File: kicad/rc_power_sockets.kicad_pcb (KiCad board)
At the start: 2 copper layers, 50 x 50 mm, 20 parts, among them IC1 ATTINY85, J1 PIR, J2 433MHZ, J3 433MHZ, P1 ICSP, P2 CONN_GND, Q1 NMOS, Q2 PMOS, SW1 SPST, U1 MCP1700T

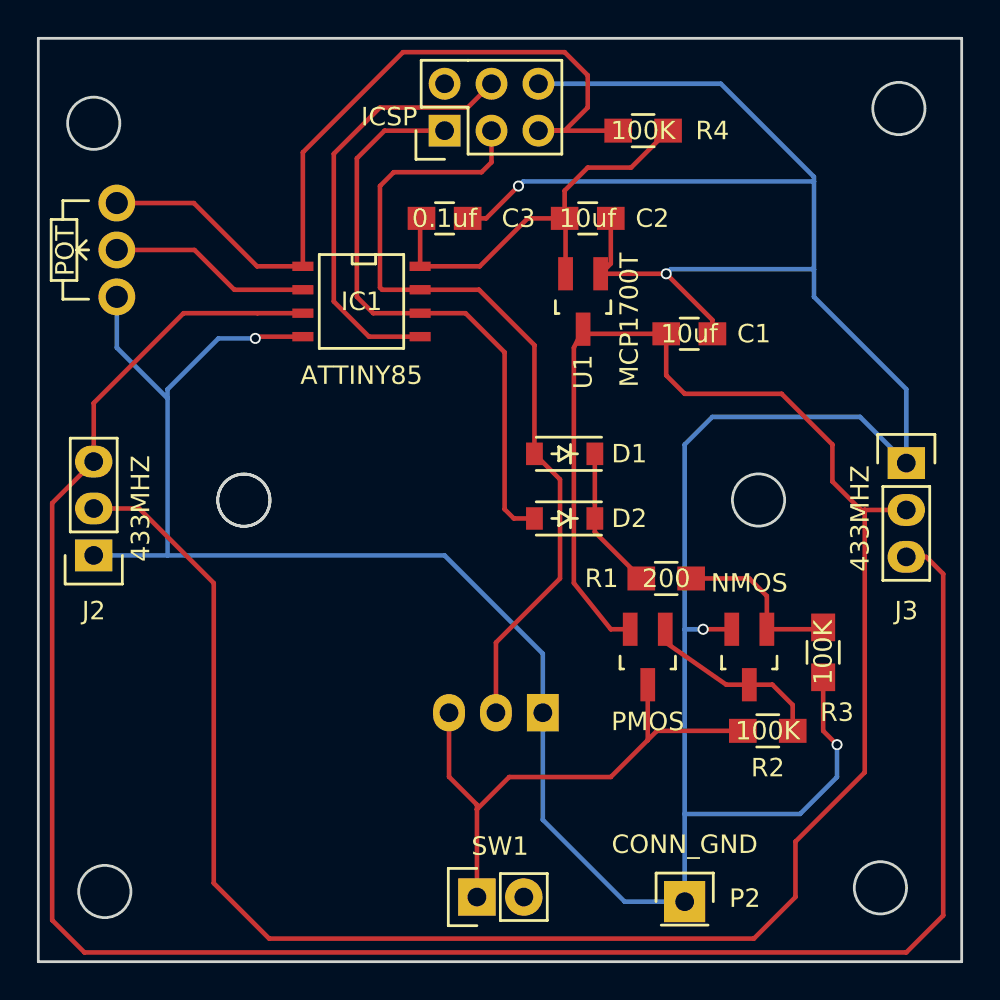
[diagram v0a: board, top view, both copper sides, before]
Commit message: Switched power plane
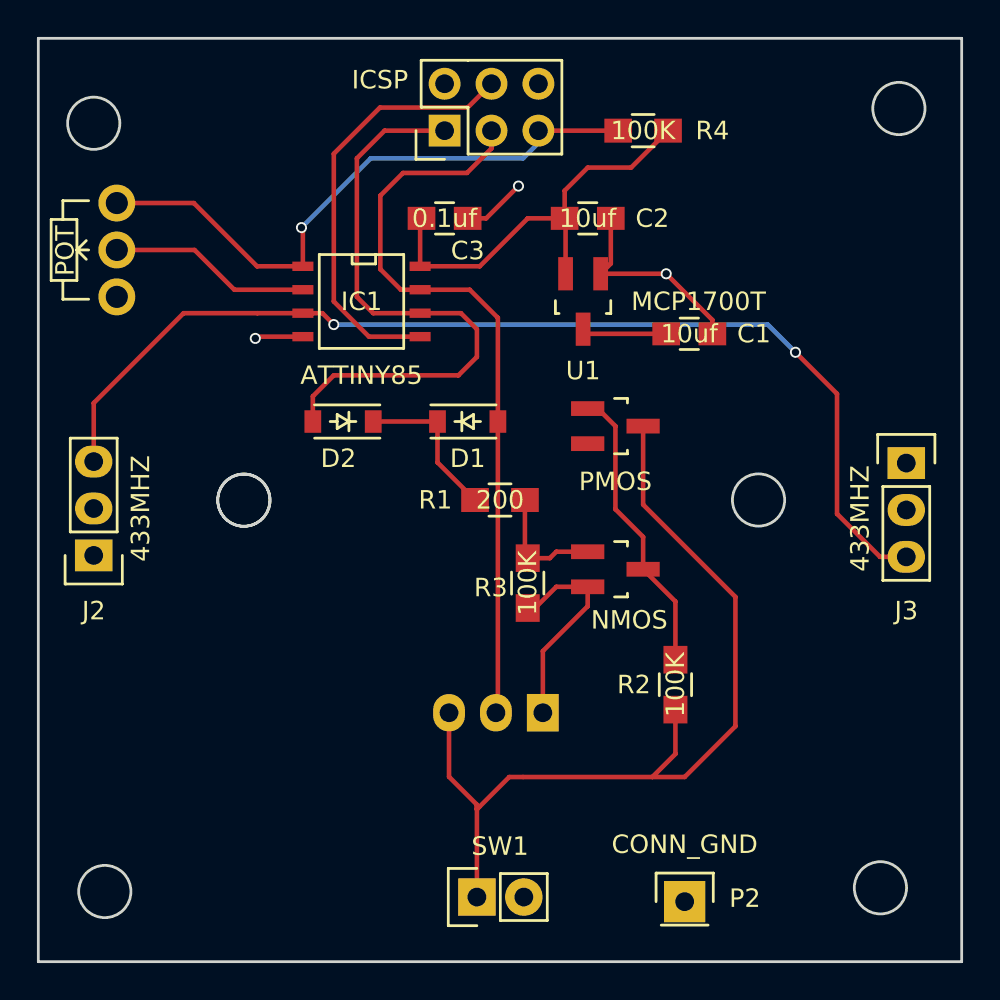
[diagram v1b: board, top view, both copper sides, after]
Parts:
- moved R3 16.4 mm to (146.5, 89.5)
- moved D2 13.1 mm to (136.5, 80.8)
- moved Q2 12.6 mm to (151.2, 81.0), turned to 270 degrees
- moved R1 9.95 mm to (145.0, 85.0)
- moved Q1 8.67 mm to (151.2, 88.8), turned to 270 degrees
- moved R2 5.59 mm to (154.5, 95.0), turned to 90 degrees
- moved D1 5.53 mm to (143.2, 80.8), turned to 0 degrees
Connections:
- P1 pad 2: /POWER -> /SWITCH_POWER
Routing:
- net GND: track 198.3 -> 28.7 mm, vias 5 -> 3
- net /SWITCH_POWER: track 122.9 -> 4.60 mm
- net /RADIO_DATA: track 113.0 -> 59.0 mm, vias 0 -> 2
- net /POWER: track 29.8 -> 49.2 mm
- net /RESET: track 45.1 -> 33.3 mm, vias 0 -> 1
- net /PBASE: track 10.2 -> 15.9 mm
- net /SCK: track 45.4 -> 40.9 mm
- net /NBASE: track 9.38 -> 6.61 mm
- net /NBASE_ON: track 7.79 -> 8.57 mm
- added copper zone on F.Cu, net /SWITCH_POWER
- added copper zone on B.Cu, net GND

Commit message: Mounting holes
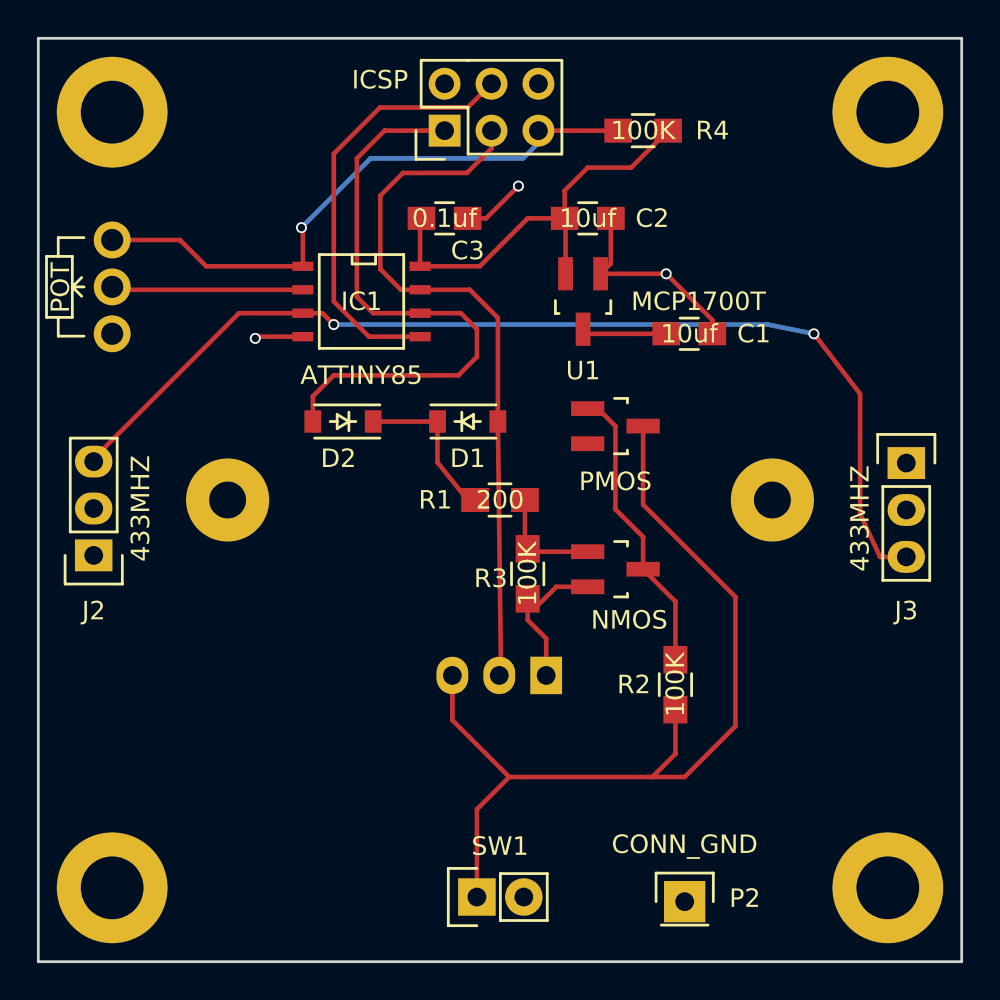
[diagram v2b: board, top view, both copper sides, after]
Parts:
- added REF**: SolderWirePad_single_2mmDrill, Wire_Pads:SolderWirePad_single_2mmDrill, F.Cu at (130.2, 85.0)
- added REF**: SolderWirePad_single_2-5mmDrill, Wire_Pads:SolderWirePad_single_2-5mmDrill, F.Cu at (124.0, 106.0)
- added REF**: SolderWirePad_single_2-5mmDrill, Wire_Pads:SolderWirePad_single_2-5mmDrill, F.Cu at (124.0, 64.0)
- added REF**: SolderWirePad_single_2-5mmDrill, Wire_Pads:SolderWirePad_single_2-5mmDrill, F.Cu at (166.0, 64.0)
- added REF**: SolderWirePad_single_2-5mmDrill, Wire_Pads:SolderWirePad_single_2-5mmDrill, F.Cu at (166.0, 106.0)
- added REF**: SolderWirePad_single_2mmDrill, Wire_Pads:SolderWirePad_single_2mmDrill, F.Cu at (159.8, 85.0)
- moved J1 2.03 mm to (147.5, 94.5)
- moved RV1 2.02 mm to (124.0, 76.0)
- moved R3 0.50 mm to (146.5, 89.0)
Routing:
- net GND: track 28.7 -> 25.4 mm
- net /SCK: track 40.9 -> 39.6 mm
- net /RADIO_DATA: track 59.0 -> 57.9 mm
- net /POWER: track 49.2 -> 49.9 mm
- net /NBASE: track 6.61 -> 6.02 mm
- net /RESET: track 33.3 -> 32.8 mm
- net /ADC3: track 11.0 -> 10.4 mm
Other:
- outline, holes or cut-outs redrawn

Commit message: Grounded mounting holes
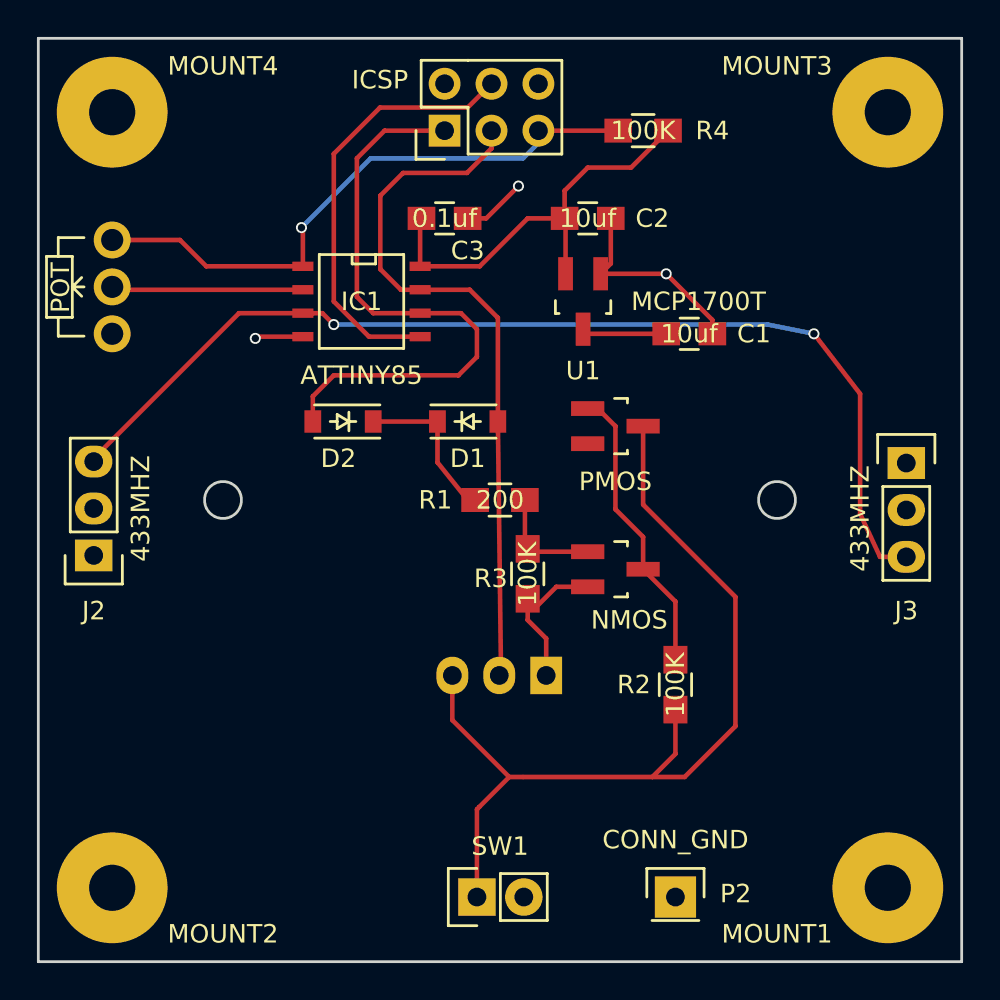
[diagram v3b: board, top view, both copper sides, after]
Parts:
- removed REF** (x2): SolderWirePad_single_2mmDrill, Wire_Pads:SolderWirePad_single_2mmDrill
- removed REF** (x4): SolderWirePad_single_2-5mmDrill, Wire_Pads:SolderWirePad_single_2-5mmDrill
- added MOUNT1: CONN_01X01, Wire_Pads:SolderWirePad_single_2-5mmDrill, F.Cu at (166.0, 106.0)
- added MOUNT2: CONN_01X01, Wire_Pads:SolderWirePad_single_2-5mmDrill, F.Cu at (124.0, 106.0)
- added MOUNT3: CONN_01X01, Wire_Pads:SolderWirePad_single_2-5mmDrill, F.Cu at (166.0, 64.0)
- added MOUNT4: CONN_01X01, Wire_Pads:SolderWirePad_single_2-5mmDrill, F.Cu at (124.0, 64.0)
- moved P2 0.56 mm to (154.5, 106.5)
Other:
- outline, holes or cut-outs redrawn
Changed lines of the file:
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@@
 (kicad_pcb (version 4) (host pcbnew 4.0.2-4+6225~38~ubuntu14.04.1-stable)
   (general
-    (links 42)
+    (links 46)
     (no_connects 0)
-    (area 112.185475 57.795 180.354525 112.055)
+    (area 118.375 59.924999 172.378334 112.055)
     (thickness 1.6)
-    (drawings 5)
+    (drawings 7)
     (tracks 117)
     (zones 0)
-    (modules 26)
+    (modules 24)
     (nets 15)
   )
@@
     (add_net VCC)
   )
-  (module Wire_Pads:SolderWirePad_single_2mmDrill (layer F.Cu)
-    (at 130.25 85)
-    (fp_text reference REF** (at 0 -3.81) (layer F.SilkS) hide
-      (effects (font (size 1 1) (thickness 0.15)))
-    )
-    (fp_text value SolderWirePad_single_2mmDrill (at -0.635 3.81) (layer F.Fab) hide
-      (effects (font (size 1 1) (thickness 0.15)))
-    )
-    (pad 1 thru_hole circle (at 0 0) (size 4.50088 4.50088) (drill 1.99898) (layers *.Cu *.Mask F.SilkS))
-  )
-  (module Wire_Pads:SolderWirePad_single_2-5mmDrill (layer F.Cu)
-    (at 124 106)
-    (fp_text reference REF** (at 0 -5.08) (layer F.SilkS) hide
-      (effects (font (size 1 1) (thickness 0.15)))
-    )
-    (fp_text value SolderWirePad_single_2-5mmDrill (at 1.27 5.08) (layer F.Fab) hide
-      (effects (font (size 1 1) (thickness 0.15)))
-    )
-    (pad 1 thru_hole circle (at 0 0) (size 5.99948 5.99948) (drill 3.4) (layers *.Cu *.Mask F.SilkS))
-  )
-  (module Wire_Pads:SolderWirePad_single_2-5mmDrill (layer F.Cu)
-    (at 124 64)
-    (fp_text reference REF** (at 0 -5.08) (layer F.SilkS) hide
-      (effects (font (size 1 1) (thickness 0.15)))
-    )
-    (fp_text value SolderWirePad_single_2-5mmDrill (at 1.27 5.08) (layer F.Fab) hide
-      (effects (font (size 1 1) (thickness 0.15)))
-    )
-    (pad 1 thru_hole circle (at 0 0) (size 5.99948 5.99948) (drill 3.4) (layers *.Cu *.Mask F.SilkS))
-  )
-  (module Wire_Pads:SolderWirePad_single_2-5mmDrill (layer F.Cu)
-    (at 166 64)
-    (zone_connect 1)
-    (fp_text reference REF** (at 0 -5.08) (layer F.SilkS) hide
-      (effects (font (size 1 1) (thickness 0.15)))
-    )
-    (fp_text value SolderWirePad_single_2-5mmDrill (at 1.27 5.08) (layer F.Fab) hide
-      (effects (font (size 1 1) (thickness 0.15)))
-    )
-    (pad 1 thru_hole circle (at 0 0) (size 5.99948 5.99948) (drill 3.4) (layers *.Cu *.Mask F.SilkS)
-      (zone_connect 1))
-  )
   (module TO_SOT_Packages_SMD:SOT-23_Handsoldering (layer F.Cu)
     (at 151.25 88.75 270)
@@
   )
   (module Pin_Headers:Pin_Header_Straight_1x01 (layer F.Cu)
-    (at 155 106.75)
+    (at 154.5 106.5)
     (descr "Through hole pin header")
     (tags "pin header")
@@
   (module Wire_Pads:SolderWirePad_single_2-5mmDrill (layer F.Cu)
     (at 166 106)
-    (fp_text reference REF** (at 0 -5.08) (layer F.SilkS) hide
-      (effects (font (size 1 1) (thickness 0.15)))
-    )
-    (fp_text value SolderWirePad_single_2-5mmDrill (at 1.27 5.08) (layer F.Fab) hide
-      (effects (font (size 1 1) (thickness 0.15)))
-    )
-    (pad 1 thru_hole circle (at 0 0) (size 5.99948 5.99948) (drill 3.4) (layers *.Cu *.Mask F.SilkS))
-  )
-  (module Wire_Pads:SolderWirePad_single_2mmDrill (layer F.Cu)
-    (at 159.75 85)
-    (fp_text reference REF** (at 0 -3.81) (layer F.SilkS) hide
-      (effects (font (size 1 1) (thickness 0.15)))
-    )
-    (fp_text value SolderWirePad_single_2mmDrill (at -0.635 3.81) (layer F.Fab) hide
-      (effects (font (size 1 1) (thickness 0.15)))
-    )
-    (pad 1 thru_hole circle (at 0 0) (size 4.50088 4.50088) (drill 1.99898) (layers *.Cu *.Mask F.SilkS))
-  )
+    (fp_text reference MOUNT1 (at -6 2.5) (layer F.SilkS)
+      (effects (font (size 1 1) (thickness 0.15)))
+    )
+    (fp_text value CONN_01X01 (at 1.27 5.08) (layer F.Fab) hide
+      (effects (font (size 1 1) (thickness 0.15)))
+    )
+    (pad 1 thru_hole circle (at 0 0) (size 5.99948 5.99948) (drill 2.49936) (layers *.Cu *.Mask F.SilkS)
+      (net 1 GND))
+  )
+  (module Wire_Pads:SolderWirePad_single_2-5mmDrill (layer F.Cu)
+    (at 124 106)
+    (fp_text reference MOUNT2 (at 6 2.5) (layer F.SilkS)
+      (effects (font (size 1 1) (thickness 0.15)))
+    )
+    (fp_text value CONN_01X01 (at 1.27 5.08) (layer F.Fab) hide
+      (effects (font (size 1 1) (thickness 0.15)))
+    )
+    (pad 1 thru_hole circle (at 0 0) (size 5.99948 5.99948) (drill 2.49936) (layers *.Cu *.Mask F.SilkS)
+      (net 1 GND))
+  )
+  (module Wire_Pads:SolderWirePad_single_2-5mmDrill (layer F.Cu)
+    (at 166 64)
+    (fp_text reference MOUNT3 (at -6 -2.5) (layer F.SilkS)
+      (effects (font (size 1 1) (thickness 0.15)))
+    )
+    (fp_text value CONN_01X01 (at 1.27 5.08) (layer F.Fab) hide
+      (effects (font (size 1 1) (thickness 0.15)))
+    )
+    (pad 1 thru_hole circle (at 0 0) (size 5.99948 5.99948) (drill 2.49936) (layers *.Cu *.Mask F.SilkS)
+      (net 1 GND))
+  )
+  (module Wire_Pads:SolderWirePad_single_2-5mmDrill (layer F.Cu)
+    (at 124 64)
+    (fp_text reference MOUNT4 (at 6 -2.5) (layer F.SilkS)
+      (effects (font (size 1 1) (thickness 0.15)))
+    )
+    (fp_text value CONN_01X01 (at 1.27 5.08 90) (layer F.Fab) hide
+      (effects (font (size 1 1) (thickness 0.15)))
+    )
+    (pad 1 thru_hole circle (at 0 0) (size 5.99948 5.99948) (drill 2.49936) (layers *.Cu *.Mask F.SilkS)
+      (net 1 GND))
+  )
+  (gr_circle (center 130 85) (end 130 84) (layer Edge.Cuts) (width 0.15))
+  (gr_circle (center 160 85) (end 160 84) (layer Edge.Cuts) (width 0.15))
   (gr_line (start 120 85) (end 170 85) (angle 90) (layer B.SilkS) (width 0.2))
   (gr_line (start 120 110) (end 120 60) (angle 90) (layer Edge.Cuts) (width 0.15))

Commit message: Labels on connectors
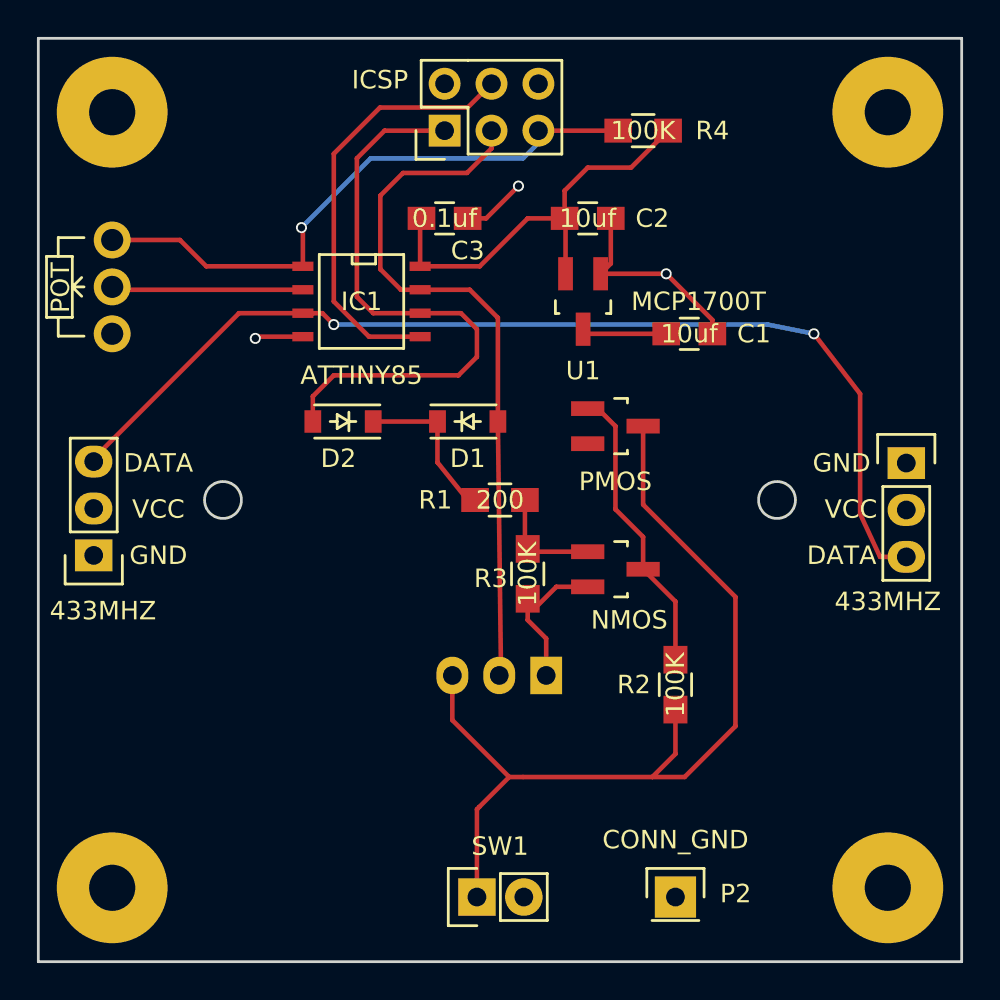
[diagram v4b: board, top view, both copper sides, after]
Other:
- board text added: "DATA"
- board text added: "GND"
- board text added: "OUT"
- board text added: "VCC"
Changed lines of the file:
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@@
     (area 118.375 59.924999 172.378334 112.055)
     (thickness 1.6)
-    (drawings 7)
+    (drawings 17)
     (tracks 117)
     (zones 0)
@@
     (descr "Through hole socket strip")
     (tags "socket strip")
-    (fp_text reference J2 (at -3 0 180) (layer F.SilkS)
-      (effects (font (size 1 1) (thickness 0.15)))
-    )
-    (fp_text value 433MHZ (at 2.54 2.54 90) (layer F.SilkS)
+    (fp_text reference J2 (at -3 0 180) (layer F.SilkS) hide
+      (effects (font (size 1 1) (thickness 0.15)))
+    )
+    (fp_text value 433MHZ (at -3 0.5 180) (layer F.SilkS)
       (effects (font (size 1 1) (thickness 0.15)))
     )
@@
     (descr "Through hole socket strip")
     (tags "socket strip")
-    (fp_text reference J3 (at 8 0 360) (layer F.SilkS)
-      (effects (font (size 1 1) (thickness 0.15)))
-    )
-    (fp_text value 433MHZ (at 3 2.5 270) (layer F.SilkS)
+    (fp_text reference J3 (at 8 0 360) (layer F.SilkS) hide
+      (effects (font (size 1 1) (thickness 0.15)))
+    )
+    (fp_text value 433MHZ (at 7.5 1 360) (layer F.SilkS)
       (effects (font (size 1 1) (thickness 0.15)))
     )
@@
   (module Wire_Pads:SolderWirePad_single_2-5mmDrill (layer F.Cu)
     (at 166 106)
-    (fp_text reference MOUNT1 (at -6 2.5) (layer F.SilkS)
+    (fp_text reference MOUNT1 (at -6 2.5) (layer F.SilkS) hide
       (effects (font (size 1 1) (thickness 0.15)))
     )
@@
   (module Wire_Pads:SolderWirePad_single_2-5mmDrill (layer F.Cu)
     (at 124 106)
-    (fp_text reference MOUNT2 (at 6 2.5) (layer F.SilkS)
+    (fp_text reference MOUNT2 (at 6 2.5) (layer F.SilkS) hide
       (effects (font (size 1 1) (thickness 0.15)))
     )
@@
   (module Wire_Pads:SolderWirePad_single_2-5mmDrill (layer F.Cu)
     (at 166 64)
-    (fp_text reference MOUNT3 (at -6 -2.5) (layer F.SilkS)
+    (fp_text reference MOUNT3 (at -6 -2.5) (layer F.SilkS) hide
       (effects (font (size 1 1) (thickness 0.15)))
     )
@@
   (module Wire_Pads:SolderWirePad_single_2-5mmDrill (layer F.Cu)
     (at 124 64)
-    (fp_text reference MOUNT4 (at 6 -2.5) (layer F.SilkS)
+    (fp_text reference MOUNT4 (at 6 -2.5) (layer F.SilkS) hide
       (effects (font (size 1 1) (thickness 0.15)))
     )
@@
       (net 1 GND))
   )
+  (gr_text GND (at 163.5 83) (layer F.SilkS)
+    (effects (font (size 1 1) (thickness 0.15)))
+  )
+  (gr_text VCC (at 164 85.5) (layer F.SilkS)
+    (effects (font (size 1 1) (thickness 0.15)))
+  )
+  (gr_text DATA (at 163.5 88) (layer F.SilkS)
+    (effects (font (size 1 1) (thickness 0.15)))
+  )
+  (gr_text DATA (at 126.5 83) (layer F.SilkS)
+    (effects (font (size 1 1) (thickness 0.15)))
+  )
+  (gr_text GND (at 126.5 88) (layer F.SilkS)
+    (effects (font (size 1 1) (thickness 0.15)))
+  )
+  (gr_text VCC (at 126.5 85.5) (layer F.SilkS)
+    (effects (font (size 1 1) (thickness 0.15)))
+  )
+  (gr_text VCC (at 146.5 108.5) (layer B.SilkS)
+    (effects (font (size 1 1) (thickness 0.15)) (justify mirror))
+  )
+  (gr_text VCC (at 142.5 98 90) (layer B.SilkS)
+    (effects (font (size 1 1) (thickness 0.15)) (justify mirror))
+  )
+  (gr_text OUT (at 145 98 90) (layer B.SilkS)
+    (effects (font (size 1 1) (thickness 0.15)) (justify mirror))
+  )
+  (gr_text GND (at 147.5 98 90) (layer B.SilkS)
+    (effects (font (size 1 1) (thickness 0.15)) (justify mirror))
+  )
   (gr_circle (center 130 85) (end 130 84) (layer Edge.Cuts) (width 0.15))
